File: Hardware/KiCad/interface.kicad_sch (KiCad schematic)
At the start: 57 parts, among them J1 USB_C, J2 STLink, J6 UART, J7 OLED, J9 Front Panel Connector, SW10 SW_Push_45deg, SW11 SW_Push_45deg, SW12 SW_Push_45deg, SW13 SW_Push_45deg, SW14 SW_Push_45deg, SW15 SW_Push_45deg, SW16 SW_Push_45deg, SW17 SW_Push_45deg, SW18 ACZ11BRXE, SW19 F1, SW2 SW_Push_45deg, SW20 F2, SW3 SW_Push_45deg, SW4 SW_Push_45deg, SW5 SW_Push_45deg, SW6 SW_Push_45deg, SW7 SW_Push_45deg, SW8 SW_Push_45deg, SW9 SW_Push_45deg, U1 USBLC6-2

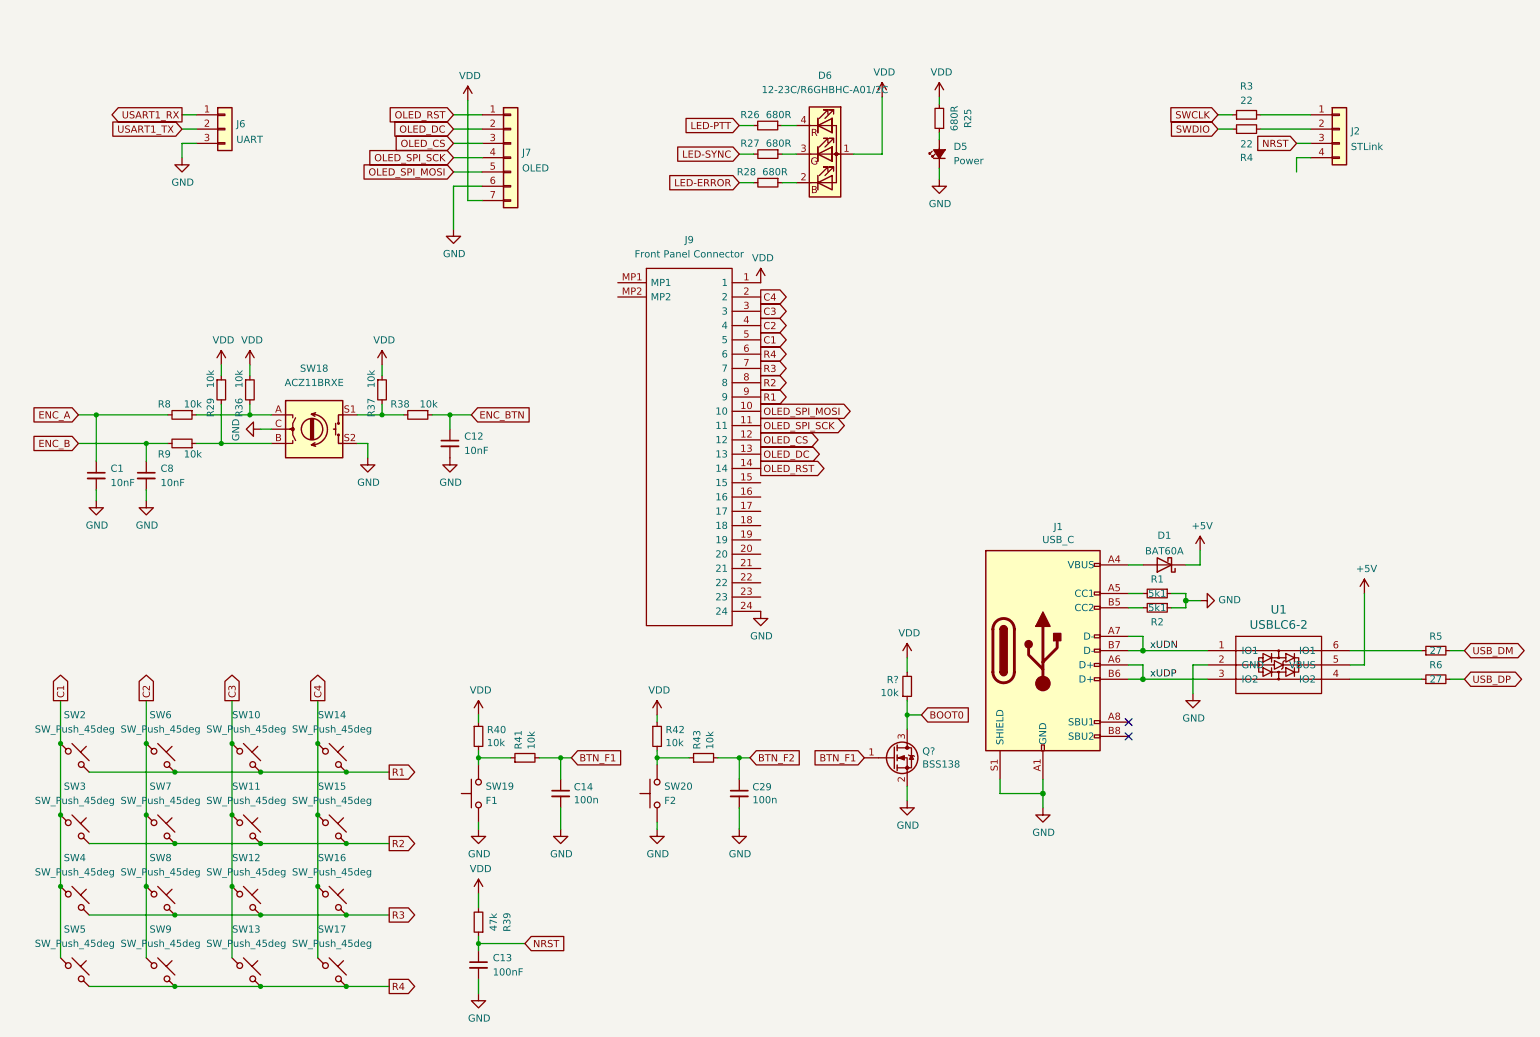
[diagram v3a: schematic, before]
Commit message: many edits throughout, added board edges for main & HMI combined, added rough layouts for some components on both
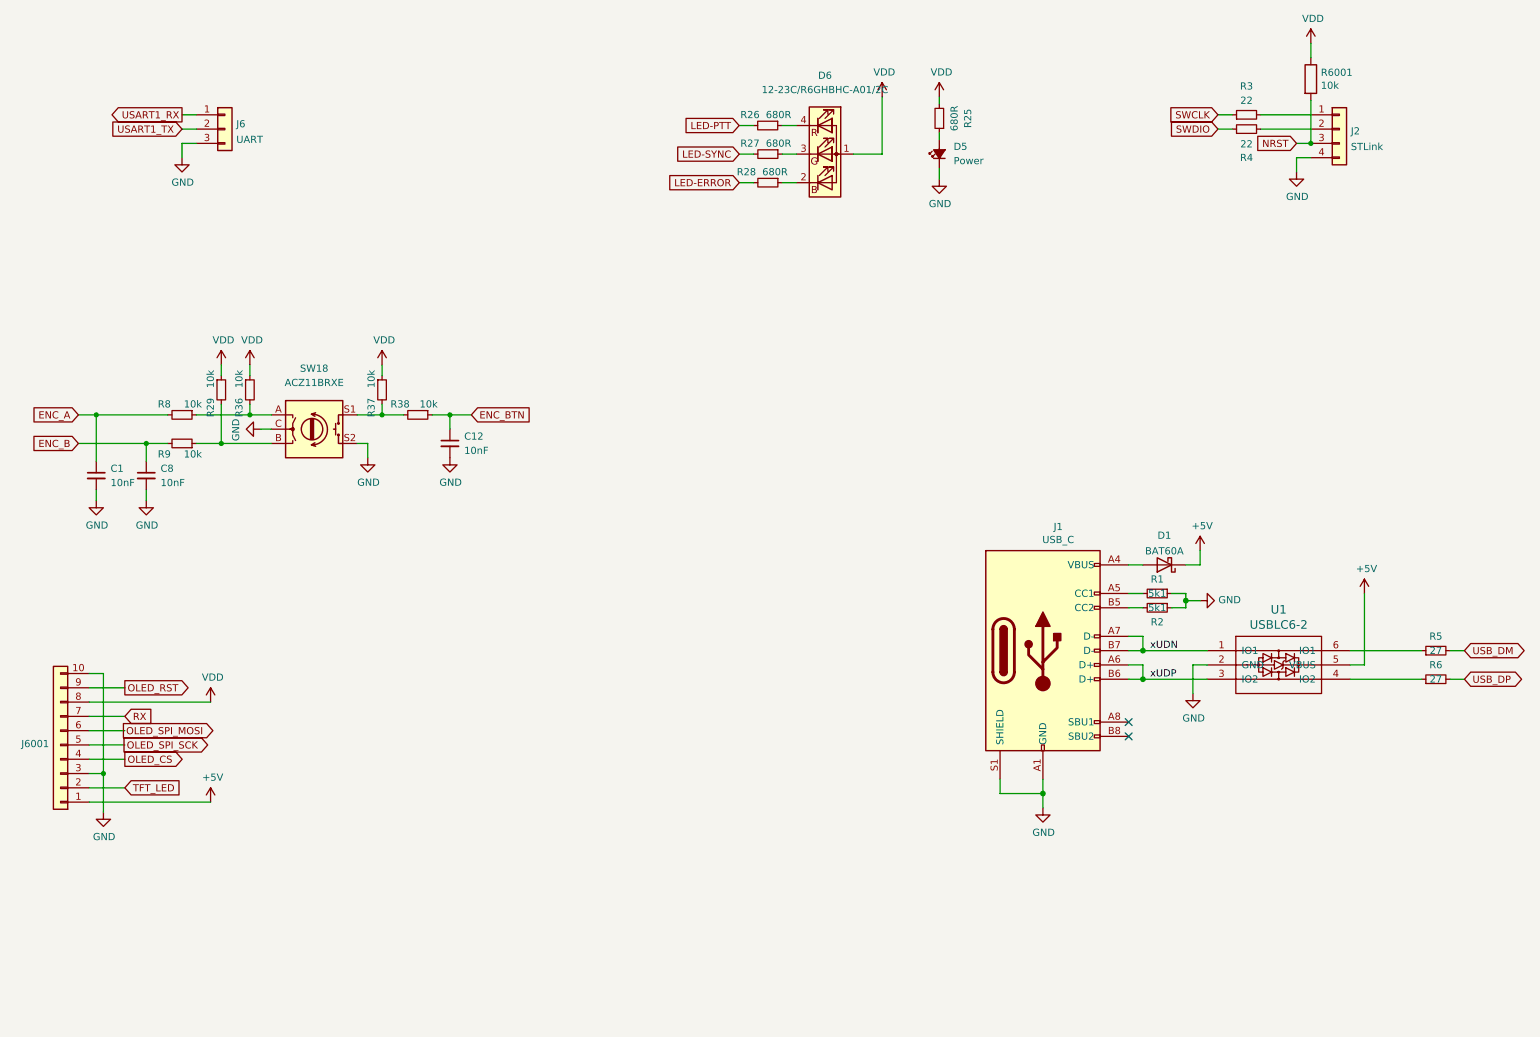
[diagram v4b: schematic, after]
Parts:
- removed C13: 100nF, Capacitor_SMD:C_0402_1005Metric, symbol Device:C_Small
- removed C14, C29: 100n, Capacitor_SMD:C_0402_1005Metric, symbol pkl_device:pkl_C_Small
- removed J7: OLED, Connector_PinHeader_2.54mm:PinHeader_1x07_P2.54mm_Vertical, symbol Connector_Generic:Conn_01x07
- removed J9: Front Panel Connector, FH19SC24S05SH09, symbol SamacSys_Parts2:FH19SC-24S-0.5SH_09_
- removed Q?: BSS138, Package_TO_SOT_SMD:SOT-23, symbol Mainboard-rescue:BSS138-Transistor_FET
- removed R39: 47k, Resistor_SMD:R_0402_1005Metric, symbol pkl_device:pkl_R_Small
- removed R40, R41, R42, R43: 10k, Resistor_SMD:R_0402_1005Metric, symbol pkl_device:pkl_R_Small
- removed R?: 10k, Resistor_SMD:R_0603_1608Metric, symbol Mainboard-rescue:R_Small-Device
- removed SW10, SW11, SW12, SW13, SW14, SW15, SW16, SW17, SW2, SW3, SW4, SW5, SW6, SW7, SW8, SW9: SW_Push_45deg, Button_Switch_SMD:SW_Push_1P1T_NO_CK_KMR2, symbol Switch:SW_Push_45deg
- removed SW19: F1, Button_Switch_THT:SW_Tactile_SPST_Angled_PTS645Vx31-2LFS, symbol Switch:SW_Push
- removed SW20: F2, Button_Switch_THT:SW_Tactile_SPST_Angled_PTS645Vx31-2LFS, symbol Switch:SW_Push
- added J6001: (no value), symbol Connector_Generic:Conn_01x10
- added R6001: 10k, Resistor_SMD:R_0603_1608Metric, symbol Device:R
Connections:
- net +5V: now also J6001.1 (Pin_1)
- net GND: now also J2.4 (Pin_4), J6001.10 (Pin_10), J6001.3 (Pin_3)
- net NRST: now also R6001.2
- net OLED_CS: now also J6001.4 (Pin_4)
- net OLED_RST: now also J6001.9 (Pin_9)
- net OLED_SPI_MOSI: now also J6001.6 (Pin_6)
- net OLED_SPI_SCK: now also J6001.5 (Pin_5)
- net VDD: now also J6001.8 (Pin_8), R6001.1
- new net RX: J6001.7 (Pin_7)
- new net TFT_LED: J6001.2 (Pin_2)
